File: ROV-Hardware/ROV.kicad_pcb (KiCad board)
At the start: 2 copper layers, 104 x 104 mm, 31 parts, among them J1 T-block, J2 T-block, J3 Screw_Terminal_01x04, SW1 switch, U1 LM7812, U2 LM7805, U3 ESP32-S3-DEVKITC-1-N8R2, U4 MPU6050, U5 ZK-BM1, U6 ZK-BM1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

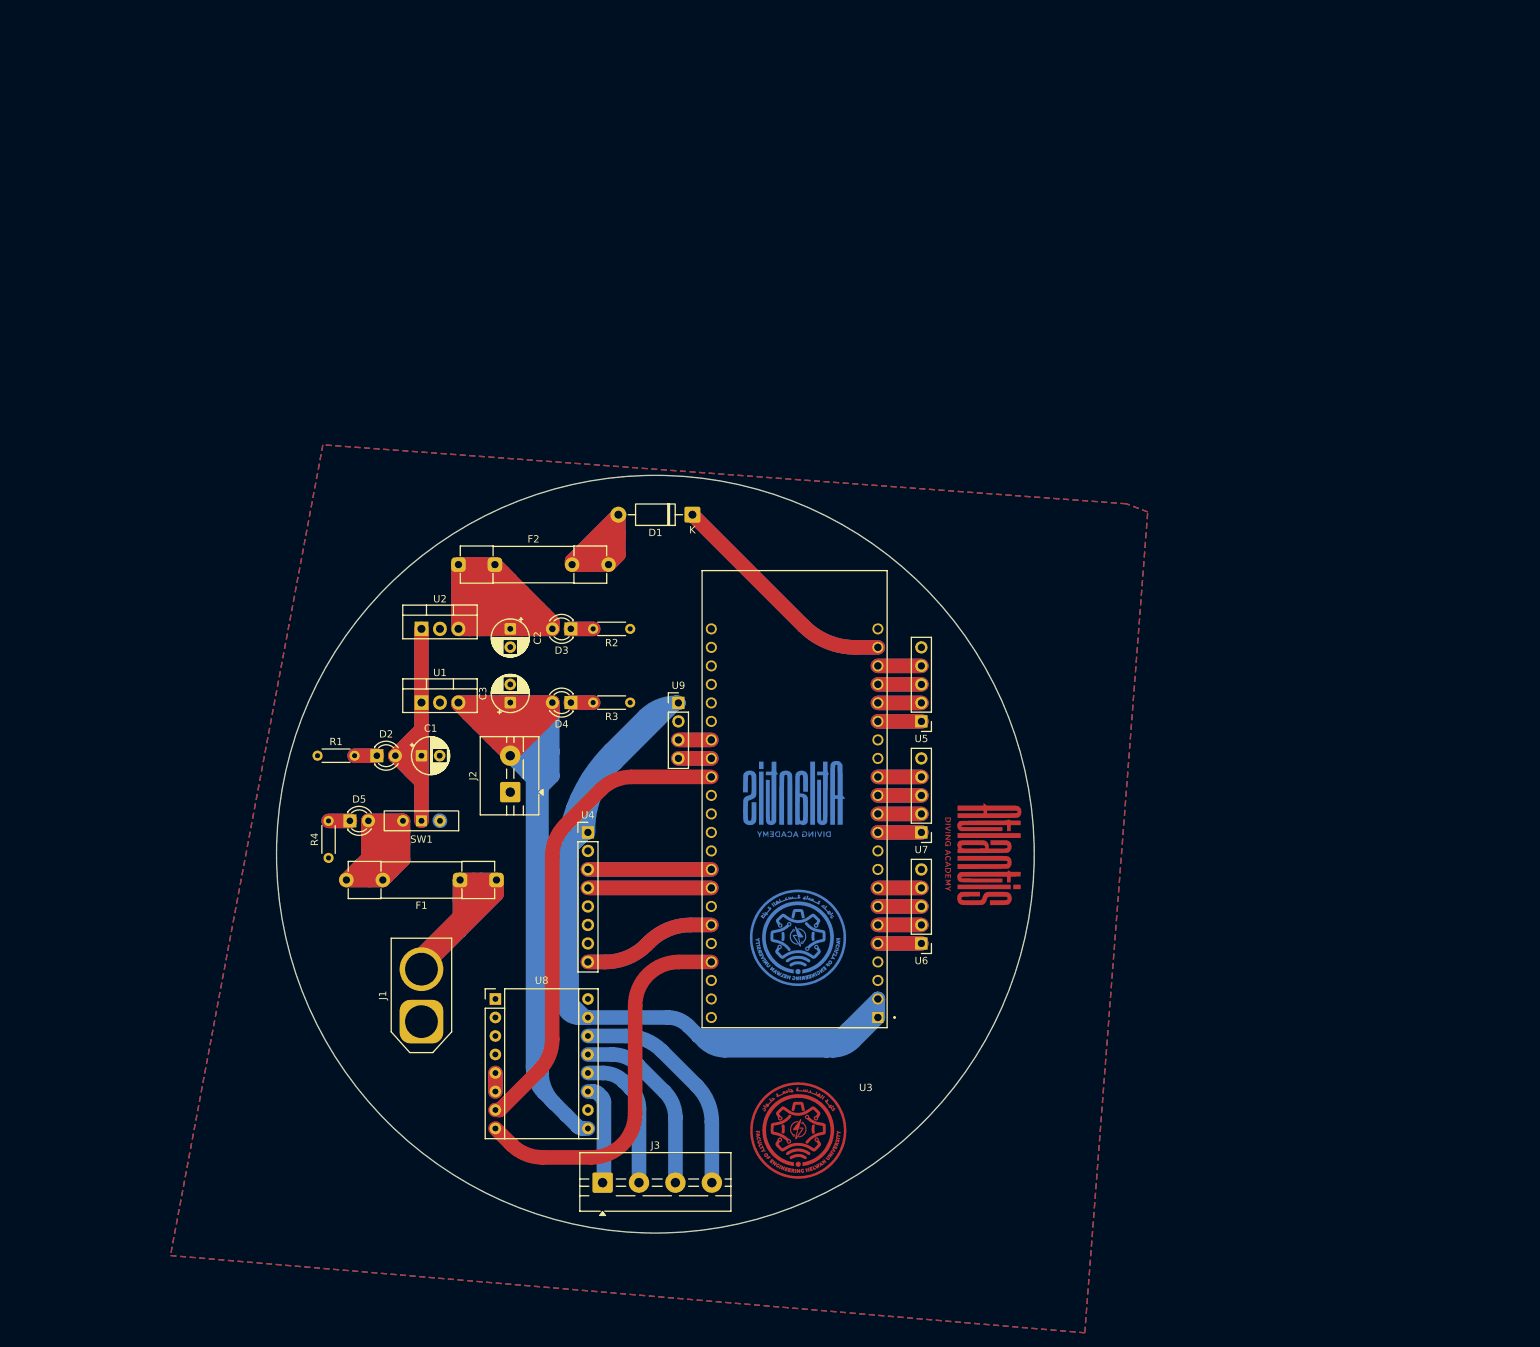
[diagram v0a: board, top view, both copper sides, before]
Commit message: editing power and grounding tracks
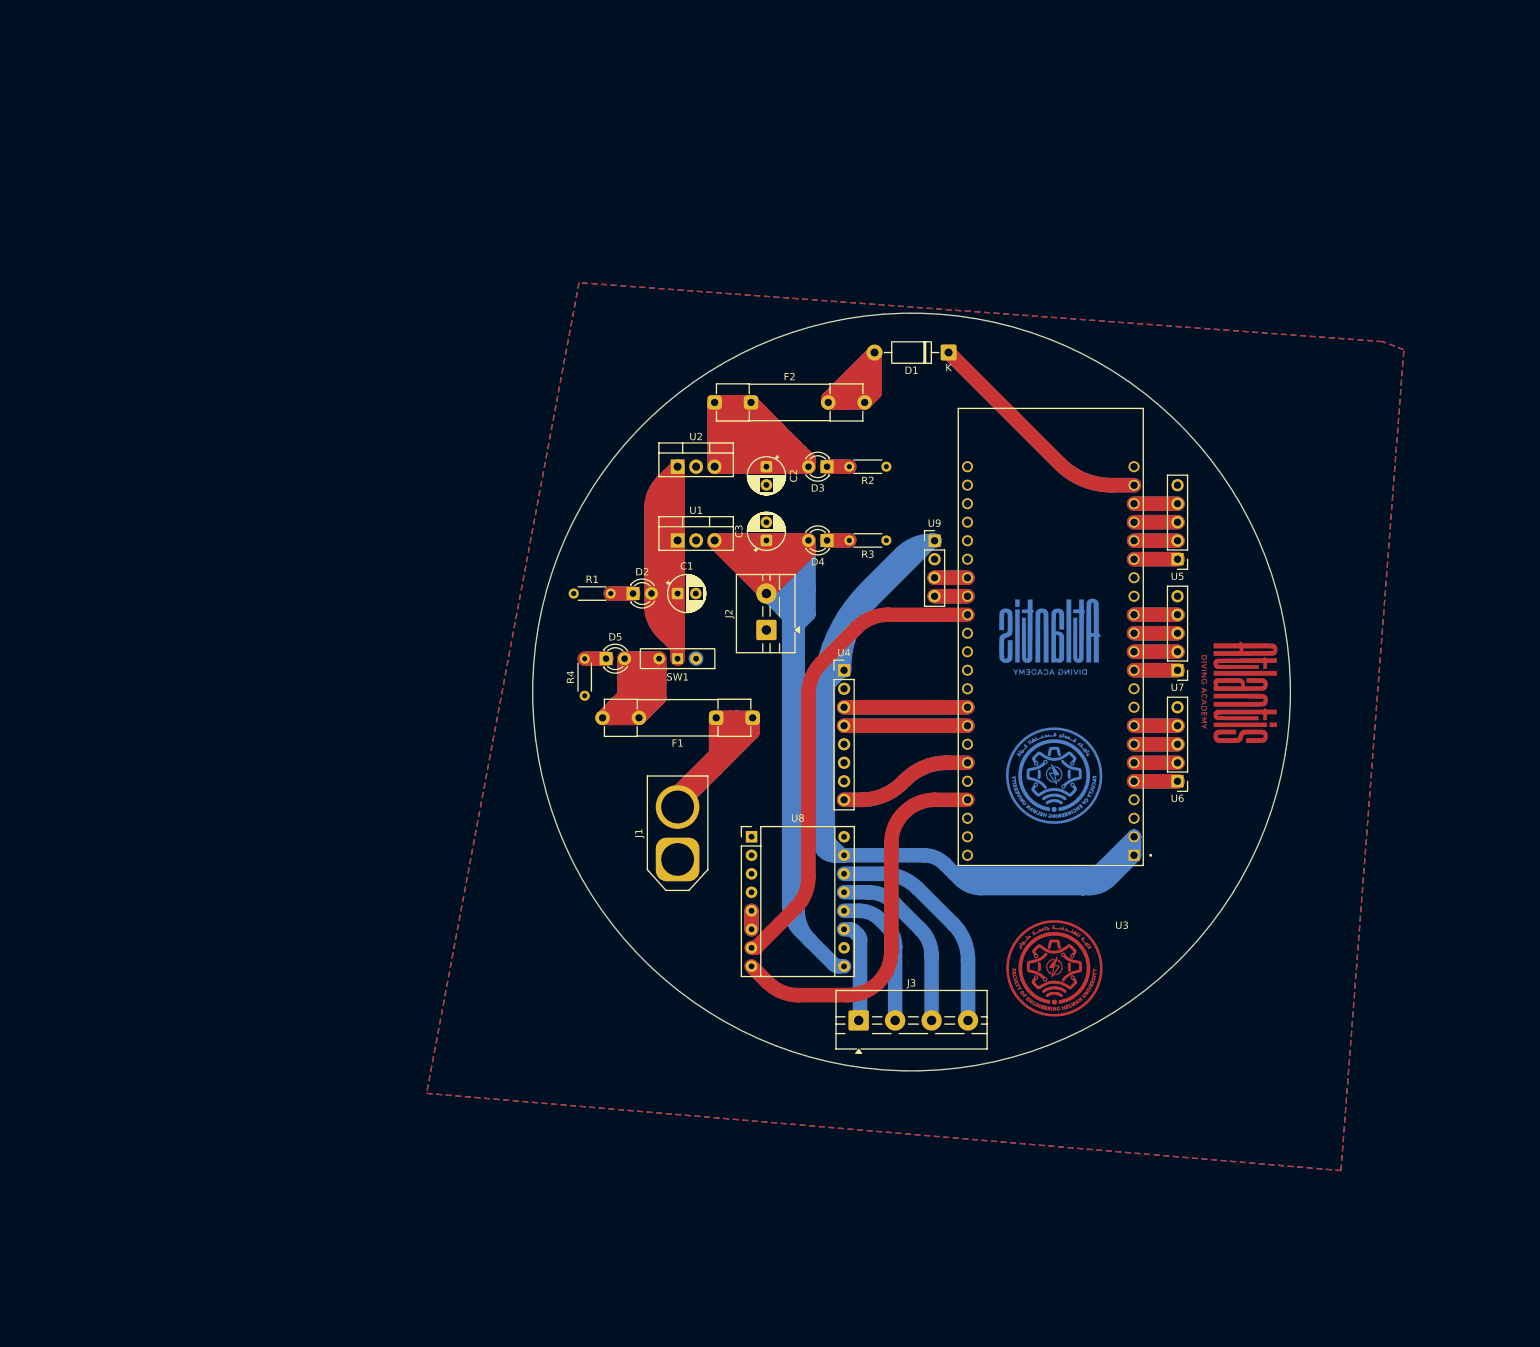
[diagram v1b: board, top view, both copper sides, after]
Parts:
- moved D3 41.6 mm to (137.8, 68.1)
- moved U4 41.6 mm to (140.2, 96.1)
- moved D4 41.6 mm to (137.8, 78.3)
- moved G*** 41.6 mm to (168.5, 92.6)
- moved U3 41.6 mm to (168.5, 91.5)
- moved C1 41.6 mm to (117.3, 85.5)
- moved D2 41.6 mm to (111.2, 85.5)
- moved D5 41.6 mm to (107.5, 94.5)
- moved F1 41.6 mm to (127.6, 102.6)
- moved F2 41.6 mm to (122.4, 59.3)
- moved J1 41.6 mm to (117.3, 122.0)
- moved R1 41.6 mm to (103.1, 85.5)
- moved R2 41.6 mm to (146.0, 68.1)
- moved R4 41.6 mm to (104.6, 99.6)
- moved SW1 41.6 mm to (117.3, 94.5)
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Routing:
- net Net-(D2-A): track 89.2 -> 217.1 mm

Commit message: water sensor
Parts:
- added U10: ~, Connector_PinHeader_2.54mm:PinHeader_1x03_P2.54mm_Vertical, F.Cu at (198.2, 96.5)
- moved G*** 48.6 mm to (141.0, 97.3), turned to 90 degrees
- moved G*** 46.3 mm to (168.3, 138.0), turned to 90 degrees
- moved U4 13.4 mm to (152.6, 91.0)
- moved G*** 2.51 mm to (169.6, 90.4), turned to -90 degrees
- turned G*** to -90 degrees
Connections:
- U3 pad J1_4: unconnected-(U3-GPIO4-PadJ1_4) -> Net-(U10-S)
- U3 pad J3_10: unconnected-(U3-GPIO38-PadJ3_10) -> Net-(U3-GPIO38)
- U3 pad J3_11: unconnected-(U3-GPIO37-PadJ3_11) -> Net-(U3-GPIO37)
- U3 pad J3_14: Net-(U3-GPIO0) -> unconnected-(U3-GPIO0-PadJ3_14)
- U3 pad J3_5: unconnected-(U3-GPIO2-PadJ3_5) -> Net-(U3-GPIO2)
- U3 pad J3_8: Net-(U3-MTDO/GPIO40) -> unconnected-(U3-MTDO/GPIO40-PadJ3_8)
- U3 pad J3_9: Net-(U3-MTCK/GPIO39) -> unconnected-(U3-MTCK/GPIO39-PadJ3_9)
- U4 pad 3: Net-(U3-MTCK/GPIO39) -> Net-(U3-GPIO37)
- U4 pad 4: Net-(U3-MTDO/GPIO40) -> Net-(U3-GPIO38)
- U8 pad 7: Net-(U3-GPIO0) -> Net-(U3-GPIO2)
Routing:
- net Net-(U3-GPIO0): track 65.3 -> 0.00 mm
- net +3.3V: track 203.6 -> 265.4 mm
- net Net-(U10-S): track 0.00 -> 59.9 mm
- net Net-(D4-A): track 297.3 -> 346.6 mm
- net Net-(U3-GPIO2): track 0.00 -> 47.6 mm
- net Net-(U3-MTDO/GPIO40): track 33.9 -> 0.00 mm
- net Net-(U3-MTCK/GPIO39): track 33.9 -> 0.00 mm
- net Net-(U3-MTMS/GPIO42): track 36.5 -> 9.04 mm
- net Net-(U3-GPIO38): track 0.00 -> 9.04 mm
- net Net-(U3-GPIO37): track 0.00 -> 9.04 mm
- net Net-(U3-GPIO1): track 52.2 -> 47.8 mm

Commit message: hight current
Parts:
- removed C3: capacitor, Capacitor_THT:CP_Radial_D5.0mm_P2.50mm
- removed D4, D5: LED, LED_THT:LED_D3.0mm
- removed G*** (x2): LOGO, logo:englogo4
- removed G*** (x2): LOGO, logo:logo7
- removed R3, R4: R, Resistor_THT:R_Axial_DIN0204_L3.6mm_D1.6mm_P5.08mm_Horizontal
- removed SW1: switch, Button_Switch_THT:SW_Slide-03_Wuerth-WS-SLTV_10x2.5x6.4_P2.54mm
- removed U1: LM7812, Package_TO_SOT_THT:TO-220-3_Vertical
- added F3: fuse, Fuse:Fuseholder_Clip-5x20mm_Schurter_CQM_Inline_P20.60x5.00mm_D1.00mm_Horizontal, F.Cu at (97.8, 81.5)
- added F4: fuse, Fuse:Fuseholder_Clip-5x20mm_Schurter_CQM_Inline_P20.60x5.00mm_D1.00mm_Horizontal, F.Cu at (97.8, 88.5)
- added F5: fuse, Fuse:Fuseholder_Clip-5x20mm_Schurter_CQM_Inline_P20.60x5.00mm_D1.00mm_Horizontal, F.Cu at (97.8, 95.4)
- J2: value T-block -> Screw_Terminal_01x04; footprint TerminalBlock:TerminalBlock_MaiXu_MX126-5.0-02P_1x02_P5.00mm -> TerminalBlock:TerminalBlock_MaiXu_MX126-5.0-04P_1x04_P5.00mm
- moved U10 94.0 mm to (130.8, 162.1), turned to -90 degrees
- moved J3 82.9 mm to (70.4, 102.6), turned to -90 degrees
- moved J1 65.0 mm to (94.4, 61.2), turned to -90 degrees
- moved J2 59.9 mm to (70.4, 81.1), turned to -90 degrees
- moved F1 43.3 mm to (104.7, 65.9), turned to -90 degrees
- moved F2 36.1 mm to (124.5, 95.4)
- moved U8 35.9 mm to (91.5, 118.8), turned to 180 degrees
- moved D1 29.6 mm to (140.1, 78.3), turned to -90 degrees
- moved U2 28.0 mm to (111.1, 95.4)
- moved C2 20.9 mm to (124.5, 88.5), turned to 0 degrees
- moved R1 18.8 mm to (121.4, 81.5), turned to 180 degrees
- moved R2 17.5 mm to (134.7, 81.5)
- moved D3 17.2 mm to (127.0, 81.5)
- moved U6 9.68 mm to (188.5, 120.7)
- moved U5 9.68 mm to (188.5, 90.2)
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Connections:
- C1 pad 1: Net-(D2-A) -> GNDREF
- C1 pad 2: GNDREF -> Net-(D2-A)
- F1 pad 2: Net-(D5-A) -> Net-(D2-A)
- J2 pad 2: Net-(D4-A) -> Net-(J2-Pin_2)
- U8 pad 7: Net-(U3-GPIO2) -> Net-(U3-GPIO1)
- U8 pad 8: Net-(U3-GPIO1) -> Net-(U3-GPIO2)
- U8 pad 9: Net-(D4-A) -> Net-(D2-A)
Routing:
- net Net-(D4-A): track 346.6 -> 0.00 mm
- net Net-(D2-A): track 217.1 -> 370.0 mm
- net Net-(D5-A): track 100.5 -> 0.00 mm
- net Net-(J2-Pin_2): track 0.00 -> 49.8 mm
- net Net-(J2-Pin_3): track 0.00 -> 47.4 mm
- net +12V: track 104.7 -> 58.8 mm
- net Net-(D3-A): track 186.7 -> 156.9 mm
- net Net-(U3-GPIO2): track 47.6 -> 75.7 mm
- net Net-(U3-GPIO1): track 47.8 -> 75.7 mm
- net +5V: track 65.0 -> 91.9 mm
- net Net-(J2-Pin_4): track 0.00 -> 24.2 mm
- net Net-(J3-Pin_4): track 31.2 -> 19.2 mm
- net Net-(J3-Pin_3): track 25.3 -> 17.6 mm
- net Net-(D1-A): track 59.3 -> 66.4 mm
- net Net-(U10-S): track 59.9 -> 66.8 mm
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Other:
- board size 104 x 104 mm -> 135 x 135 mm

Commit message: refresh
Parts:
- added G***: LOGO, logo:logo5, F.Cu at (115.5, 123.9)
- added G***: LOGO, logo:englogo, F.Cu at (128.2, 53.7)
- added G***: LOGO, logo:englogo, B.Cu at (128.2, 53.7)
- added G***: LOGO, logo:logo5, B.Cu at (115.5, 123.9)

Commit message: Fuse
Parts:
- F1, F3, F4, F5: footprint Fuse:Fuseholder_Clip-5x20mm_Schurter_CQM_Inline_P20.60x5.00mm_D1.00mm_Horizontal -> Fuse:Fuse_Blade_ATO_directSolder
- moved F5 6.17 mm to (91.6, 95.8)
- moved F4 6.16 mm to (91.6, 88.7)
- moved F3 6.16 mm to (91.6, 81.6)
- moved F1 2.77 mm to (103.5, 68.4)
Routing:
- net Net-(D2-A): track 370.0 -> 286.6 mm
- net +12V: track 58.8 -> 18.2 mm
- net Net-(J2-Pin_4): track 24.2 -> 48.2 mm
- net Net-(J2-Pin_3): track 47.4 -> 39.0 mm
- net Net-(J2-Pin_2): track 49.8 -> 54.3 mm

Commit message: DC jack
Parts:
- removed the G*** at (128.2, 53.7) (x2)
- added J4: Barrel_Jack_Switch, Connector_BarrelJack:BarrelJack_Horizontal, F.Cu at (124.5, 61.2)
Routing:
- net Net-(D3-A): track 156.9 -> 197.5 mm

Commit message: fishs and starfishs
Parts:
- added G***: LOGO, logo:fish, F.Cu at (128.8, 153.1)
- added G***: LOGO, logo:starfish, F.Cu at (89.4, 134.3)
- added G***: LOGO, logo:fish, F.Cu at (115.4, 158.3)
- added G***: LOGO, logo:starfish, F.Cu at (163.2, 57.4)
- added G***: LOGO, logo:starfish, F.Cu at (141.0, 46.9)
- added G***: LOGO, logo:starfish, F.Cu at (138.9, 142.8)
- added G***: LOGO, logo:fish, F.Cu at (121.3, 146.2)
- added G***: LOGO, logo:fish, F.Cu at (81.8, 59.4)
- added G***: LOGO, logo:fish, B.Cu at (115.6, 71.4)
- added G***: LOGO, logo:fish, B.Cu at (125.4, 41.8)
- added G***: LOGO, logo:fish, B.Cu at (163.6, 59.0)
- added G***: LOGO, logo:fish, F.Cu at (109.3, 138.5)
- added G***: LOGO, logo:fish, B.Cu at (146.8, 43.5)
- added G***: LOGO, logo:starfish, B.Cu at (116.7, 151.0)
- added G***: LOGO, logo:starfish, B.Cu at (141.4, 59.9)
- added G***: LOGO, logo:fish, B.Cu at (138.8, 127.6)
- added G***: LOGO, logo:starfish, B.Cu at (152.4, 151.5)
- added G***: LOGO, logo:starfish, B.Cu at (110.3, 49.5)
- added G***: LOGO, logo:fish, F.Cu at (113.4, 44.6)
- added G***: LOGO, logo:fish, F.Cu at (124.0, 137.7)
- added G***: LOGO, logo:fish, F.Cu at (109.4, 53.6)
- added G***: LOGO, logo:fish, F.Cu at (80.7, 68.3)
- added G***: LOGO, logo:fish, F.Cu at (145.2, 65.4)
- added G***: LOGO, logo:fish, F.Cu at (106.1, 148.2)
- J4: value Barrel_Jack_Switch -> T-block; footprint Connector_BarrelJack:BarrelJack_Horizontal -> TerminalBlock:TerminalBlock_MaiXu_MX126-5.0-02P_1x02_P5.00mm
- moved J4 5.00 mm to (119.5, 61.2), turned to 0 degrees
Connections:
- J4 pad 1: Net-(D3-A) -> GNDREF
- J4 pad 2: GNDREF -> Net-(D3-A)

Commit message: وجع القلب
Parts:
- U10: moved to B.Cu
- moved U10 5.08 mm to (125.7, 162.1)
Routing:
- net Net-(U10-S): track 66.8 -> 71.9 mm
